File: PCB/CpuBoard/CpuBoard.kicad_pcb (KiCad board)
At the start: 2 copper layers, 15 parts, among them J1 ProgUSB, J2 Conn_01x20_Male, J3 Conn_01x20_Male, SW1 SW_Reset, U1 P8X32A-Q44, U2 24LC512, Y1 5MHz

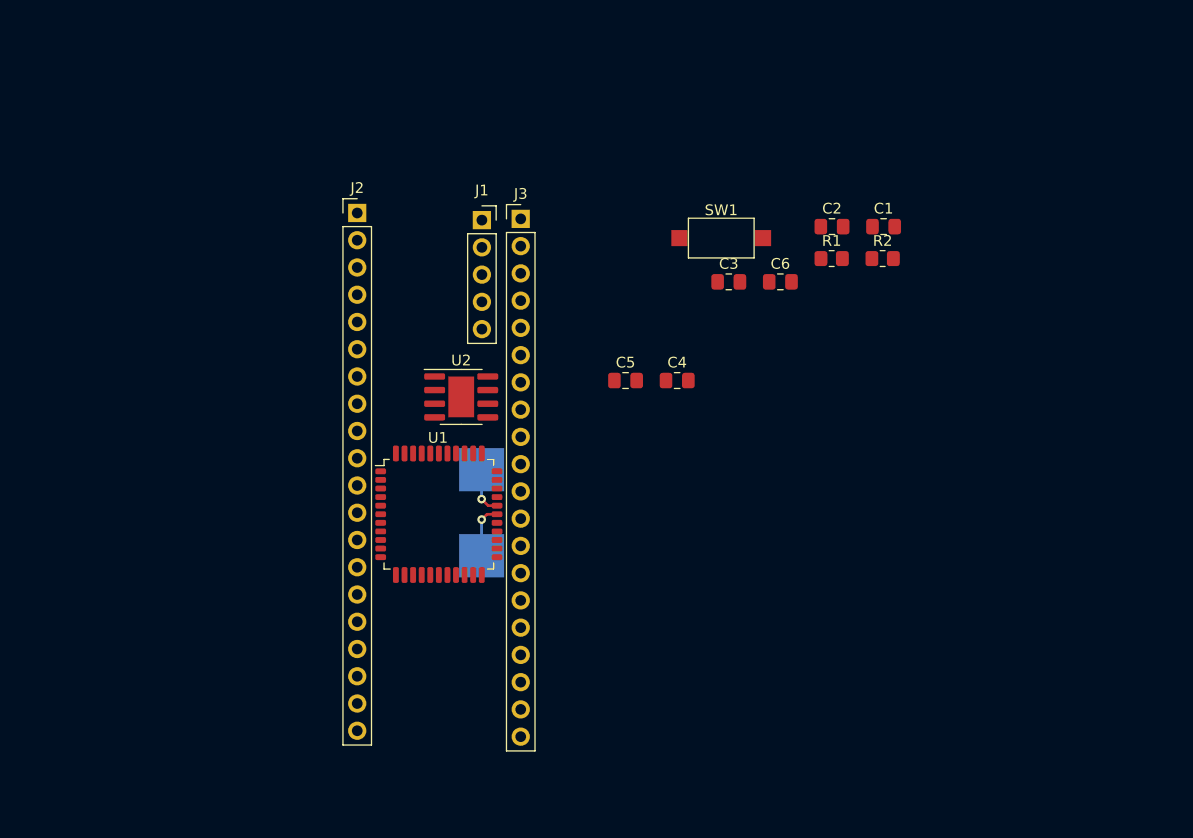
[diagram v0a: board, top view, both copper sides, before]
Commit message: Modif PCB + Datasheet
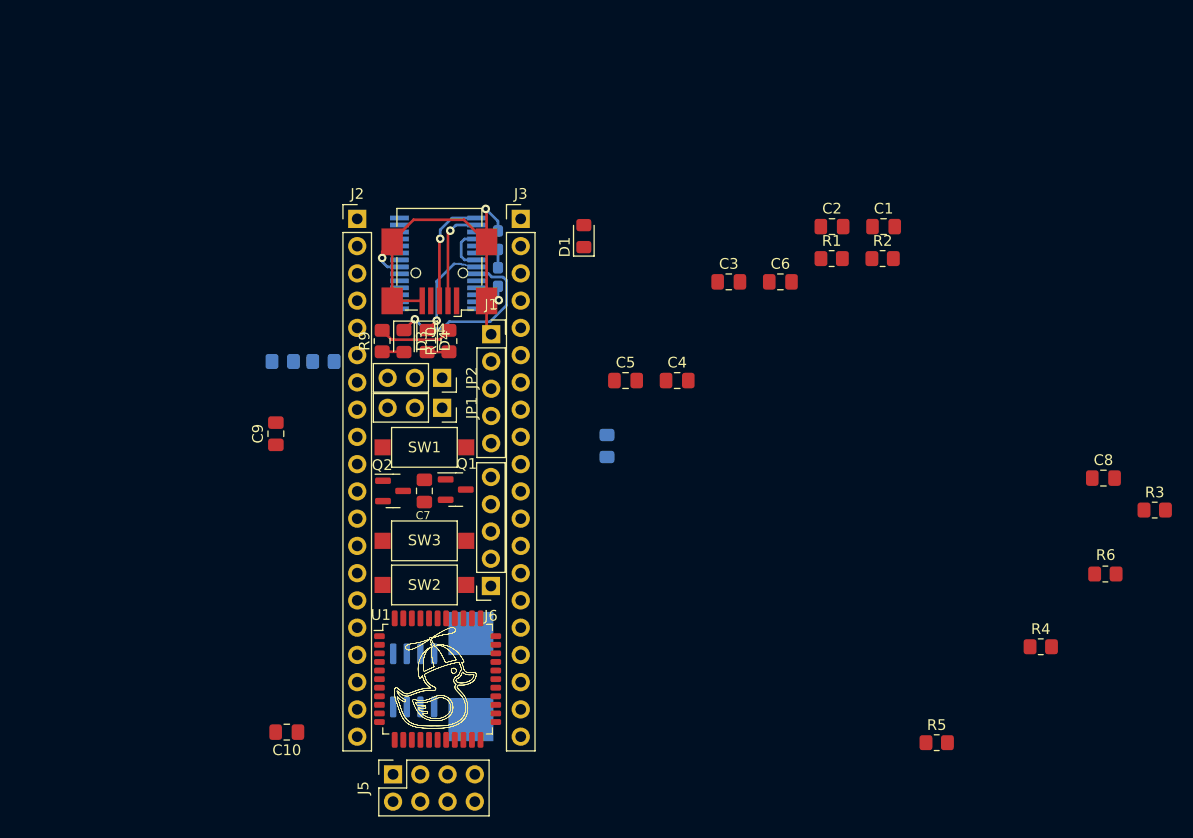
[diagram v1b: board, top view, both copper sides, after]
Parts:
- added C10: 0.1µF, Capacitor_SMD:C_0805_2012Metric_Pad1.18x1.45mm_HandSolder, F.Cu at (43.4, 92.8)
- added C11: 1µF, Capacitor_SMD:C_0603_1608Metric_Pad1.08x0.95mm_HandSolder, B.Cu at (63.1, 47.0)
- added C12: 0.1µF, Capacitor_SMD:C_0603_1608Metric_Pad1.08x0.95mm_HandSolder, B.Cu at (63.1, 50.4)
- added C7: 0.01µF, Capacitor_SMD:C_0805_2012Metric_Pad1.18x1.45mm_HandSolder, F.Cu at (56.3, 70.4)
- added C8: 0.01µF, Capacitor_SMD:C_0805_2012Metric_Pad1.18x1.45mm_HandSolder, F.Cu at (119.5, 69.2)
- added C9: 1µF, Capacitor_SMD:C_0805_2012Metric_Pad1.18x1.45mm_HandSolder, F.Cu at (42.4, 65.0)
- added D1: D_Schottky, Diode_SMD:D_0805_2012Metric_Pad1.15x1.40mm_HandSolder, F.Cu at (71.1, 46.6)
- added D2: D_Schottky, Diode_SMD:D_0805_2012Metric_Pad1.15x1.40mm_HandSolder, B.Cu at (73.3, 66.2)
- added D3: LED_RX, Diode_SMD:D_0805_2012Metric_Pad1.15x1.40mm_HandSolder, F.Cu at (54.4, 56.4)
- added D4: LED_TX, Diode_SMD:D_0805_2012Metric_Pad1.15x1.40mm_HandSolder, F.Cu at (56.5, 56.4)
- added J4: USB_B_Mini, Connector_USB:USB_Mini-B_Wuerth_65100516121_Horizontal, F.Cu at (57.7, 50.0)
- added J5: Conn_ESP-01, Connector_PinSocket_2.54mm:PinSocket_2x04_P2.54mm_Vertical, F.Cu at (53.3, 96.8)
- added J6: ProgESP, Connector_PinSocket_2.54mm:PinSocket_1x05_P2.54mm_Vertical, F.Cu at (62.5, 79.2)
- added JP1: SELECT_TX_ESP_PROP, Connector_PinSocket_2.54mm:PinSocket_1x03_P2.54mm_Vertical, F.Cu at (57.9, 62.6)
- added JP2: SELECT_RX_ESP_PROP, Connector_PinSocket_2.54mm:PinSocket_1x03_P2.54mm_Vertical, F.Cu at (57.9, 59.8)
- added Q1: MMBT3904, Package_TO_SOT_SMD:SOT-23, F.Cu at (59.2, 70.2)
- added Q2: MMBT3904, Package_TO_SOT_SMD:SOT-23, F.Cu at (53.3, 70.4)
- added R10: 330, Resistor_SMD:R_0805_2012Metric_Pad1.20x1.40mm_HandSolder, F.Cu at (58.5, 56.4)
- added R3: 33K, Resistor_SMD:R_0805_2012Metric_Pad1.20x1.40mm_HandSolder, F.Cu at (124.3, 72.1)
- added R4: 33K, Resistor_SMD:R_0805_2012Metric_Pad1.20x1.40mm_HandSolder, F.Cu at (113.7, 84.9)
- added R5: 4.7k, Resistor_SMD:R_0805_2012Metric_Pad1.20x1.40mm_HandSolder, F.Cu at (104.0, 93.8)
- added R6: 4.7k, Resistor_SMD:R_0805_2012Metric_Pad1.20x1.40mm_HandSolder, F.Cu at (119.7, 78.1)
- added R7: 150, Resistor_SMD:R_0805_2012Metric_Pad1.20x1.40mm_HandSolder, B.Cu at (43.1, 58.3)
- added R8: 150, Resistor_SMD:R_0805_2012Metric_Pad1.20x1.40mm_HandSolder, B.Cu at (46.8, 58.3)
- added R9: 330, Resistor_SMD:R_0805_2012Metric_Pad1.20x1.40mm_HandSolder, F.Cu at (52.3, 56.4)
- added SW2: SW_Prog, Button_Switch_SMD:SW_SPST_CK_RS282G05A3, F.Cu at (56.3, 79.1)
- added SW3: SW_Reset, Button_Switch_SMD:SW_SPST_CK_RS282G05A3, F.Cu at (56.3, 75.0)
- added U3: FT232RL, Package_SO:SSOP-28_5.3x10.2mm_P0.65mm, B.Cu at (57.5, 49.1)
- U2: moved to B.Cu
- moved SW1 33.9 mm to (56.3, 66.3)
- moved U2 26.8 mm to (55.3, 88.0), turned to 90 degrees
- moved U1 15.4 mm to (57.4, 87.8)
- moved Y1 15.3 mm to (60.6, 87.7)
- moved J1 10.7 mm to (62.5, 55.8)
- moved J2 0.55 mm to (50.0, 45.0)
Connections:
- net /P14 renamed /P14_ESP-TX
- net /P15 renamed /P15_ESP-RX
- U2 pad 1: unconnected-(U2-Pad1) -> GND
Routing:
- net GND: track 0.00 -> 51.4 mm, vias 0 -> 3
- net Net-(D3-Pad1): track 0.00 -> 16.6 mm, vias 0 -> 1
- net Net-(J4-Pad3): track 0.00 -> 10.5 mm, vias 0 -> 1
- net Net-(J4-Pad2): track 0.00 -> 9.30 mm, vias 0 -> 1
- net Net-(D4-Pad1): track 0.00 -> 8.59 mm, vias 0 -> 1
- net /3V3: track 0.00 -> 6.95 mm
- net Net-(U1-Pad28): track 5.02 -> 0.00 mm, vias 1 -> 0
- net Net-(U1-Pad29): track 4.43 -> 0.00 mm, vias 1 -> 0
- net /5V: track 0.00 -> 3.83 mm
- net Net-(D3-Pad2): track 0.00 -> 2.04 mm
- net Net-(D4-Pad2): track 0.00 -> 2.04 mm
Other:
- copper layers 2 -> 4
- board text added: "<-- Sus"

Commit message: New Revision
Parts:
- removed C4: 0.1µF, Capacitor_SMD:C_0805_2012Metric_Pad1.18x1.45mm_HandSolder
- added J7: Conn_ESP, Connector_PinHeader_2.54mm:PinHeader_1x20_P2.54mm_Vertical, B.Cu at (35.3, 30.0)
- added J8: ProgUSB_ESP, Connector_PinSocket_2.54mm:PinSocket_1x05_P2.54mm_Vertical, F.Cu at (32.6, 82.0)
- added JP3: ESP_TX, Connector_PinHeader_2.54mm:PinHeader_1x02_P2.54mm_Vertical, F.Cu at (23.8, 30.0)
- added JP4: ESP_RX, Connector_PinHeader_2.54mm:PinHeader_1x02_P2.54mm_Vertical, F.Cu at (27.5, 30.0)
- added SW4: SW_Reset, Button_Switch_SMD:SW_SPST_CK_RS282G05A3, F.Cu at (28.4, 51.8)
- C1: value 0.1µF -> 1µF
- C10, C9: footprint Capacitor_SMD:C_0805_2012Metric_Pad1.18x1.45mm_HandSolder -> Capacitor_SMD:C_0603_1608Metric_Pad1.08x0.95mm_HandSolder; moved to B.Cu
- C11: value 1µF -> 0.1µF; footprint Capacitor_SMD:C_0603_1608Metric_Pad1.08x0.95mm_HandSolder -> Capacitor_SMD:C_0805_2012Metric_Pad1.18x1.45mm_HandSolder; moved to F.Cu
- C12: value 0.1µF -> 1µF; footprint Capacitor_SMD:C_0603_1608Metric_Pad1.08x0.95mm_HandSolder -> Capacitor_SMD:C_0805_2012Metric_Pad1.18x1.45mm_HandSolder; moved to F.Cu
- C2, C3: value 0.1µF -> 0.01µF; moved to B.Cu
- C5, D1, Q1, Q2: moved to B.Cu
- C7: value 0.01µF -> 0.1µF; moved to B.Cu
- C8: value 0.01µF -> 0.1µF
- J1: value ProgUSB -> USB_B_Mini; footprint Connector_PinSocket_2.54mm:PinSocket_1x05_P2.54mm_Vertical -> Connector_USB:USB_Mini-B_Wuerth_65100516121_Horizontal
- J2: value Conn_01x20_Male -> Conn_ESP-01; footprint Connector_PinHeader_2.54mm:PinHeader_1x20_P2.54mm_Vertical -> Connector_PinSocket_2.54mm:PinSocket_2x04_P2.54mm_Vertical
- J4: value USB_B_Mini -> Conn_ESP; footprint Connector_USB:USB_Mini-B_Wuerth_65100516121_Horizontal -> Connector_PinSocket_2.54mm:PinSocket_1x20_P2.54mm_Vertical; moved to B.Cu
- J5: value Conn_ESP-01 -> ProgUSB_Pro; footprint Connector_PinSocket_2.54mm:PinSocket_2x04_P2.54mm_Vertical -> Connector_PinSocket_2.54mm:PinSocket_1x05_P2.54mm_Horizontal
- J6: value ProgESP -> Conn_01x20_Male; footprint Connector_PinSocket_2.54mm:PinSocket_1x05_P2.54mm_Vertical -> Connector_PinHeader_2.54mm:PinHeader_1x20_P2.54mm_Vertical
- JP1: value SELECT_TX_ESP_PROP -> Pro_TX; footprint Connector_PinSocket_2.54mm:PinSocket_1x03_P2.54mm_Vertical -> Connector_PinHeader_2.54mm:PinHeader_1x02_P2.54mm_Vertical
- JP2: value SELECT_RX_ESP_PROP -> Pro_RX; footprint Connector_PinSocket_2.54mm:PinSocket_1x03_P2.54mm_Vertical -> Connector_PinHeader_2.54mm:PinHeader_1x02_P2.54mm_Vertical
- R1, R2: value 10k -> 33K; moved to B.Cu
- R3, R4: value 33K -> 10k; moved to B.Cu
- SW2: value SW_Prog -> SW_Prog_ESP
- SW3: value SW_Reset -> SW_Reset_ESP
- moved R6 93.1 mm to (31.4, 48.7), turned to 180 degrees
- moved R5 90.7 mm to (25.3, 48.6), turned to 180 degrees
- moved R3 74.0 mm to (53.4, 51.2), turned to -90 degrees
- moved R4 67.3 mm to (55.4, 51.2), turned to -90 degrees
- moved C10 66.2 mm to (57.9, 28.3), turned to 0 degrees
- moved C8 59.7 mm to (59.8, 67.8), turned to 180 degrees
- moved J6 49.3 mm to (65.2, 30.0), turned to 0 degrees
- moved C1 44.1 mm to (59.8, 65.8), turned to 180 degrees
- moved SW3 43.7 mm to (28.4, 41.3), turned to 0 degrees
- moved SW2 43.7 mm to (28.4, 45.5), turned to 0 degrees
- moved R2 43.5 mm to (57.8, 62.7), turned to -90 degrees
- moved J4 42.7 mm to (20.0, 30.0)
- moved C12 39.1 mm to (25.6, 61.4), turned to 180 degrees
- moved D2 39.0 mm to (58.0, 30.2), turned to 0 degrees
- moved R1 37.0 mm to (57.4, 51.2), turned to 90 degrees
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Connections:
- C1 pad 1: /3V3 -> /Propeller/3V3
- C10 pad 1: /3V3 -> /Propeller/5V
- C11 pad 1: /5V -> /ESP-01/3V3
- C12 pad 1: /5V -> /ESP-01/3V3
- C2 pad 1: /3V3 -> /Propeller/FT232_RTS
- C2 pad 2: GND -> Net-(C2-Pad2)
- C3 pad 1: /3V3 -> /Propeller/FT232_DTR
- C3 pad 2: GND -> Net-(C3-Pad2)
- C5 pad 1: /3V3 -> /Propeller/3V3
- C6 pad 1: /3V3 -> /Propeller/3V3
- C7 pad 1: /FT232_RTS -> /Propeller/3V3
- C7 pad 2: Net-(C7-Pad2) -> GND
- C8 pad 1: /FT232_DTR -> /Propeller/3V3
- C8 pad 2: Net-(C8-Pad2) -> GND
- C9 pad 1: /3V3 -> /Propeller/5V
- D1 pad 1: /5V -> /Propeller/5V
- D2 pad 1: /3V3 -> /Propeller/3V3
- J1 pad 1: GND -> Net-(D1-Pad2)
- J1 pad 2: /Reset -> Net-(J1-Pad2)
- J1 pad 3: /P31_RX -> Net-(J1-Pad3)
- J1 pad 4: /P30_TX -> unconnected-(J1-Pad4)
- J1 pad 5: /3V3 -> GND
- J2 pad 1: /P0 -> GND
- J2 pad 2: /P1 -> /ESP-01/ESP_TX
- J2 pad 3: /P2 -> /ESP-01/P14_ESP-TX
- J2 pad 4: /P3 -> /ESP-01/3V3
- J2 pad 5: /P4 -> /ESP-01/P15_ESP-RX
- J2 pad 6: /P5 -> Net-(J2-Pad6)
- J2 pad 7: /P6 -> /ESP-01/ESP_RX
- J2 pad 8: /P7 -> /ESP-01/3V3
- J3 pad 1: /P31_RX -> /Propeller/P0
- J3 pad 10: GND -> /Propeller/3V3
- J3 pad 11: /5V -> /Propeller/Reset
- J3 pad 12: GND -> /Propeller/7-12V
- J3 pad 13: /P23 -> /Propeller/P8
- J3 pad 14: /P22 -> /Propeller/P9
- J3 pad 15: /P21 -> /Propeller/P10
- J3 pad 16: /P20 -> /Propeller/P11
- J3 pad 17: /P19 -> /Propeller/P12
- J3 pad 18: /P18 -> /Propeller/P13
- J3 pad 19: /P17 -> /Propeller/P14_ESP-TX
- J3 pad 2: /P30_TX -> /Propeller/P1
- J3 pad 20: /P16 -> /Propeller/P15_ESP-RX
- J3 pad 3: /P29_SDA -> /Propeller/P2
- J3 pad 4: /P28_SCL -> /Propeller/P3
- J3 pad 5: /P27 -> /Propeller/P4
- J3 pad 6: /P26 -> /Propeller/P5
- J3 pad 7: /P25 -> /Propeller/P6
- J3 pad 8: /P24 -> /Propeller/P7
- J3 pad 9: /3V3 -> GND
- J4 pad 1: Net-(D1-Pad2) -> unconnected-(J4-Pad1)
- J4 pad 2: Net-(J4-Pad2) -> unconnected-(J4-Pad2)
- J4 pad 3: Net-(J4-Pad3) -> unconnected-(J4-Pad3)
- J4 pad 5: GND -> unconnected-(J4-Pad5)
- J4 pad 6: GND -> unconnected-(J4-Pad6)
- J5 pad 2: /ESP_TX -> /Propeller/Reset
- J5 pad 3: /P14_ESP-TX -> /Propeller/P31_RX
- J5 pad 4: /3V3 -> /Propeller/P30_TX
- J5 pad 5: /P15_ESP-RX -> /Propeller/3V3
- J6 pad 1: GND -> /Propeller/FT232_RX
- J6 pad 2: unconnected-(J6-Pad2) -> /Propeller/FT232_TX
- J6 pad 3: /ESP_RX -> /Propeller/P29_SDA
- J6 pad 4: /ESP_TX -> /Propeller/P28_SCL
- J6 pad 5: /3V3 -> /Propeller/P27
- JP1 pad 1: /ESP_TX -> /Propeller/FT232_TX
- JP1 pad 2: /FT232_TX -> /Propeller/P31_RX
- JP2 pad 1: /ESP_RX -> /Propeller/FT232_RX
- JP2 pad 2: /FT232_RX -> /Propeller/P30_TX
- Q1 pad 1: Net-(C7-Pad2) -> Net-(C2-Pad2)
- Q1 pad 3: /Reset -> /Propeller/Reset
- Q2 pad 1: Net-(C8-Pad2) -> Net-(C3-Pad2)
- Q2 pad 3: /Reset -> /Propeller/Reset
- R1 pad 1: /3V3 -> Net-(C2-Pad2)
- R1 pad 2: /P29_SDA -> GND
- R10 pad 2: /3V3 -> /Propeller/3V3
- R2 pad 1: /3V3 -> Net-(C3-Pad2)
- R2 pad 2: /P28_SCL -> GND
- R3 pad 1: Net-(C7-Pad2) -> /Propeller/3V3
- R3 pad 2: GND -> /Propeller/P29_SDA
- R4 pad 1: Net-(C8-Pad2) -> /Propeller/3V3
- R4 pad 2: GND -> /Propeller/P28_SCL
- R5 pad 1: /3V3 -> /ESP-01/3V3
- R5 pad 2: /P15_ESP-RX -> /ESP-01/P15_ESP-RX
- R6 pad 1: /3V3 -> /ESP-01/3V3
- R6 pad 2: Net-(J5-Pad6) -> Net-(J2-Pad6)
- R7 pad 2: /FT232_TX -> /Propeller/FT232_TX
- R8 pad 2: /FT232_RX -> /Propeller/FT232_RX
- R9 pad 2: /3V3 -> /Propeller/3V3
- SW1 pad 2: /Reset -> /Propeller/Reset
- SW2 pad 1: /P15_ESP-RX -> /ESP-01/P15_ESP-RX
- SW3 pad 1: Net-(J5-Pad6) -> Net-(J2-Pad6)
- U1 pad 1: /P4 -> /Propeller/P4
- U1 pad 10: /P9 -> /Propeller/P9
- U1 pad 11: /P10 -> /Propeller/P10
- U1 pad 12: /P11 -> /Propeller/P11
- U1 pad 13: /P12 -> /Propeller/P12
- U1 pad 14: /P13 -> /Propeller/P13
- U1 pad 15: /P14_ESP-TX -> /Propeller/P14_ESP-TX
- U1 pad 16: /P15_ESP-RX -> /Propeller/P15_ESP-RX
- U1 pad 18: /3V3 -> /Propeller/3V3
- U1 pad 19: /P16 -> /Propeller/P16
- U1 pad 2: /P5 -> /Propeller/P5
- U1 pad 20: /P17 -> /Propeller/P17
- U1 pad 21: /P18 -> /Propeller/P18
- U1 pad 22: /P19 -> /Propeller/P19
- U1 pad 23: /P20 -> /Propeller/P20
- U1 pad 24: /P21 -> /Propeller/P21
- U1 pad 25: /P22 -> /Propeller/P22
- U1 pad 26: /P23 -> /Propeller/P23
- U1 pad 3: /P6 -> /Propeller/P6
- U1 pad 30: /3V3 -> /Propeller/3V3
- U1 pad 31: /P24 -> /Propeller/P24
- U1 pad 32: /P25 -> /Propeller/P25
- U1 pad 33: /P26 -> /Propeller/P26
- U1 pad 34: /P27 -> /Propeller/P27
- U1 pad 35: /P28_SCL -> /Propeller/P28_SCL
- U1 pad 36: /P29_SDA -> /Propeller/P29_SDA
- U1 pad 37: /P30_TX -> /Propeller/P30_TX
- U1 pad 38: /P31_RX -> /Propeller/P31_RX
- U1 pad 4: /P7 -> /Propeller/P7
- U1 pad 40: /3V3 -> /Propeller/3V3
- U1 pad 41: /P0 -> /Propeller/P0
- U1 pad 42: /P1 -> /Propeller/P1
- U1 pad 43: /P2 -> /Propeller/P2
- U1 pad 44: /P3 -> /Propeller/P3
- U1 pad 7: /Reset -> /Propeller/Reset
- U1 pad 8: /3V3 -> /Propeller/3V3
- U1 pad 9: /P8 -> /Propeller/P8
- U2 pad 5: /P29_SDA -> /Propeller/P29_SDA
- U2 pad 6: /P28_SCL -> /Propeller/P28_SCL
- U2 pad 8: /3V3 -> /Propeller/3V3
- U3 pad 15: Net-(J4-Pad3) -> Net-(J1-Pad3)
- U3 pad 16: Net-(J4-Pad2) -> Net-(J1-Pad2)
- U3 pad 2: /FT232_DTR -> /Propeller/FT232_DTR
- U3 pad 20: /5V -> /Propeller/5V
- U3 pad 3: /FT232_RTS -> /Propeller/FT232_RTS
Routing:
- net GND: track 51.4 -> 228.3 mm, vias 3 -> 11
- net /Propeller/3V3: track 0.00 -> 99.3 mm, vias 0 -> 3
- net /ESP-01/3V3: track 0.00 -> 61.5 mm
- net /ESP-01/ESP_TX: track 0.00 -> 61.4 mm
- net /Propeller/Reset: track 0.00 -> 59.5 mm
- net /ESP-01/ESP_RX: track 0.00 -> 59.1 mm
- net /Propeller/5V: track 0.00 -> 58.2 mm, vias 0 -> 1
- net /Propeller/P30_TX: track 0.00 -> 44.0 mm
- net /Propeller/P31_RX: track 0.00 -> 42.4 mm
- net /ESP-01/P15_ESP-RX: track 0.00 -> 39.8 mm
- net /Propeller/P29_SDA: track 0.00 -> 31.1 mm, vias 0 -> 1
- net /Propeller/P28_SCL: track 0.00 -> 29.4 mm, vias 0 -> 1
- net /Propeller/FT232_TX: track 0.00 -> 26.9 mm
- net Net-(J2-Pad6): track 0.00 -> 26.8 mm
- net Net-(C2-Pad2): track 0.00 -> 25.6 mm
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
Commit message: Finished v0.1
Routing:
- net /ESP-01/3V3: track 61.5 -> 63.6 mm
- net /ESP-01/ESP_TX: track 61.4 -> 63.3 mm
